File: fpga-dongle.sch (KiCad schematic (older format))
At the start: 118 parts, among them P1 CONN_01X02, P2 PGM, P3 right, P4 left, P5 CONN_01X40, P6 CONN_01X40, P7 DBG_SWD, P8 USB_PWR, Q1 BC857, SW1 T1107A(6x3,8x2,5MM)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

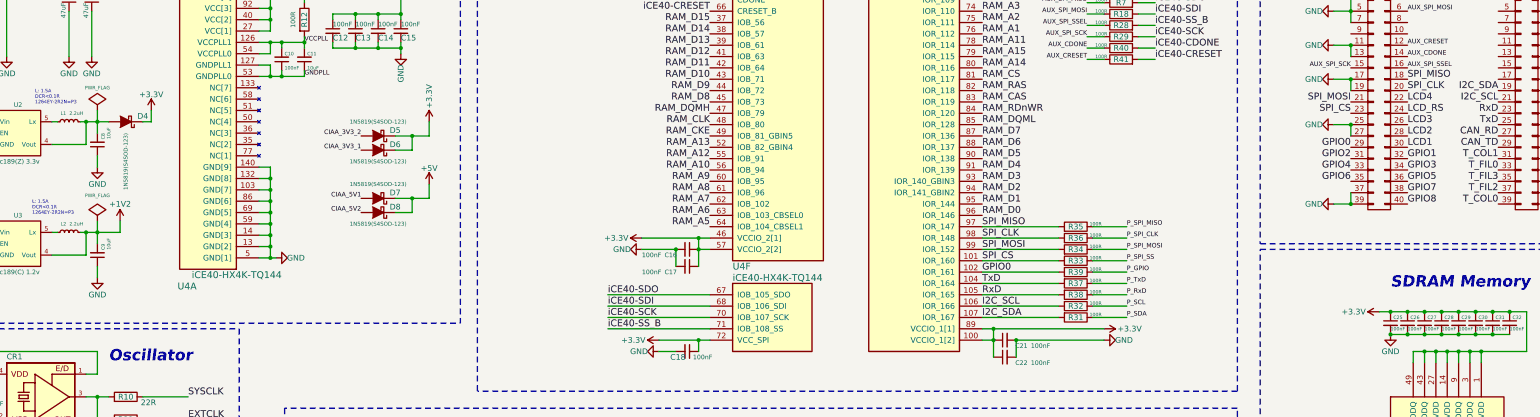
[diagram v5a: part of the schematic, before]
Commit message: Remove unnecesary components and clean power supply
Signed-off-by: Martin Ribelotta <martinribelotta@gmail.com>
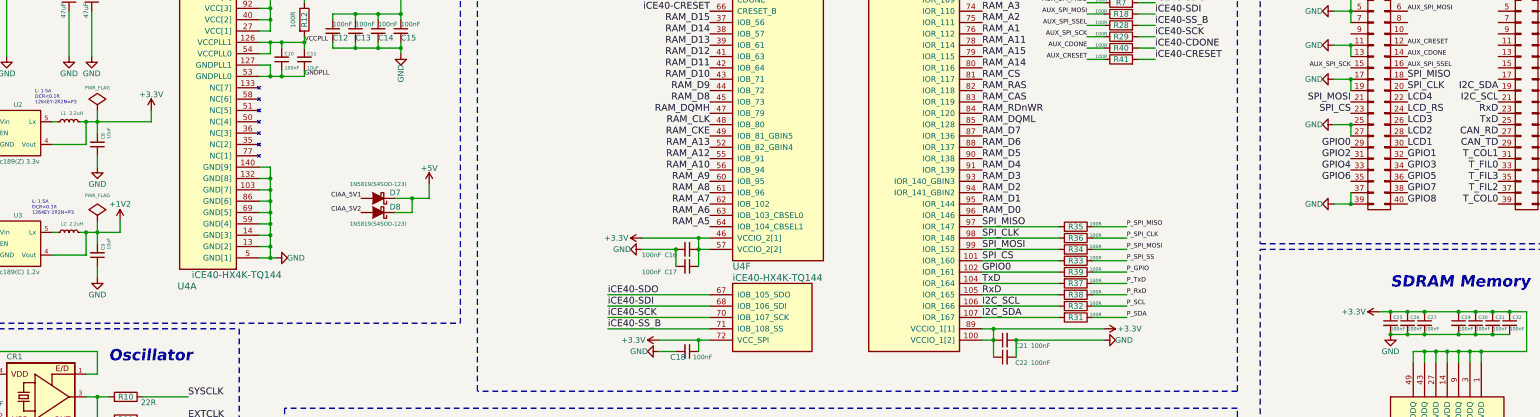
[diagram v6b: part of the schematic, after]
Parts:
- removed C28: 100nF, Capacitors_SMD:C_0805, symbol C_Small
- removed D4, D5, D6: 1N5819(S4SOD-123), Diodes_SMD:SOD-123, symbol D_Schottky
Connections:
- net +3V3: now also C8.2, L1.2, U2.4 (Vout)
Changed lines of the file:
@@
-$EndComp
-$Comp
-L C_Small C28
-U 1 1 57D74400
-P 14600 4375
-F 0 "C28" H 14625 4425 30  0000 L CNN
-F 1 "100nF" H 14600 4325 30  0000 L CNN
-F 2 "Capacitors_SMD:C_0805" H 14600 4375 50  0001 C CNN
-F 3 "" H 14600 4375 50  0000 C CNN
-	1    14600 4375
-	1    0    0    -1
 $EndComp
 $Comp
@@
 Connection ~ 14900 4275
 Connection ~ 14750 4275
-Connection ~ 14600 4275
 Connection ~ 14450 4275
 Connection ~ 14300 4275
@@
 Connection ~ 14550 7925
 Connection ~ 14450 7925
-Connection ~ 14600 4475
 Connection ~ 14750 4475
 Connection ~ 14900 4475
@@
 	2650 2800 2650 2600
 Wire Wire Line
-	2600 2600 2850 2600
+	2600 2600 3225 2600
 Connection ~ 2650 2600
 Wire Wire Line
@@
 Text Label 13800 1425 2    40   ~ 0
 CIAA_3V3_2
-Text Label 5075 2725 2    40   ~ 0
-CIAA_3V3_2
-Text Label 5075 2850 2    40   ~ 0
-CIAA_3V3_1
-$Comp
-L D_Schottky D4
-U 1 1 57F214FE
-P 3000 2600
-F 0 "D4" H 2850 2550 50  0000 C CNN
-F 1 "1N5819(S4SOD-123)" V 3000 2950 35  0000 C CNN
-F 2 "Diodes_SMD:SOD-123" H 3000 2600 60  0001 C CNN
-F 3 "" H 3000 2600 60  0000 C CNN
-	1    3000 2600
-	-1   0    0    1
-$EndComp
-Wire Wire Line
-	3225 2500 3225 2600
-Wire Wire Line
-	3225 2600 3150 2600
-$Comp
-L D_Schottky D5
-U 1 1 57F2204B
-P 5225 2725
-F 0 "D5" H 5075 2675 50  0000 C CNN
-F 1 "1N5819(S4SOD-123)" H 5225 2600 35  0000 C CNN
-F 2 "Diodes_SMD:SOD-123" H 5225 2725 60  0001 C CNN
-F 3 "" H 5225 2725 60  0000 C CNN
-	1    5225 2725
-	-1   0    0    1
-$EndComp
-$Comp
-L D_Schottky D6
-U 1 1 57F227C6
-P 5225 2850
-F 0 "D6" H 5075 2800 50  0000 C CNN
-F 1 "1N5819(S4SOD-123)" H 5225 2950 35  0000 C CNN
-F 2 "Diodes_SMD:SOD-123" H 5225 2850 60  0001 C CNN
-F 3 "" H 5225 2850 60  0000 C CNN
-	1    5225 2850
-	-1   0    0    1
-$EndComp
-Wire Wire Line
-	5375 2725 5675 2725
-Wire Wire Line
-	5525 2725 5525 2850
-Wire Wire Line
-	5525 2850 5375 2850
-Wire Wire Line
-	5675 2725 5675 2600
-Connection ~ 5525 2725
+Wire Wire Line
+	3225 2600 3225 2500
 $Comp
 L +3.3V #PWR092
-U 1 1 57F232E2
-P 5675 2600
-F 0 "#PWR092" H 5675 2450 50  0001 C CNN
-F 1 "+3.3V" V 5675 2825 50  0000 C CNN
-F 2 "" H 5675 2600 60  0000 C CNN
-F 3 "" H 5675 2600 60  0000 C CNN
-	1    5675 2600
-	-1   0    0    -1
-$EndComp
-$Comp
-L +3.3V #PWR093
 U 1 1 57F24EE1
 P 1450 3475
-F 0 "#PWR093" H 1450 3325 50  0001 C CNN
+F 0 "#PWR092" H 1450 3325 50  0001 C CNN
 F 1 "+3.3V" H 1450 3615 50  0000 C CNN
 F 2 "" H 1450 3475 60  0000 C CNN
@@
 CIAA_5V2
 $Comp
-L +5V #PWR094
+L +5V #PWR093
 U 1 1 57F2DD2B
 P 5675 3150
-F 0 "#PWR094" H 5675 3000 50  0001 C CNN
+F 0 "#PWR093" H 5675 3000 50  0001 C CNN
 F 1 "+5V" H 5675 3290 50  0000 C CNN
 F 2 "" H 5675 3150 60  0000 C CNN
@@
 	3200 1050 3200 1125
 $Comp
-L +5V #PWR095
+L +5V #PWR094
 U 1 1 57F32DD8
 P 12425 12625
-F 0 "#PWR095" H 12425 12475 50  0001 C CNN
+F 0 "#PWR094" H 12425 12475 50  0001 C CNN
 F 1 "+5V" H 12425 12765 50  0000 C CNN
 F 2 "" H 12425 12625 60  0000 C CNN
@@
 	12425 12625 12425 12700
 $Comp
-L +5V #PWR096
+L +5V #PWR095
 U 1 1 57F340DA
 P 1125 2100
-F 0 "#PWR096" H 1125 1950 50  0001 C CNN
+F 0 "#PWR095" H 1125 1950 50  0001 C CNN
 F 1 "+5V" H 1125 2240 50  0000 C CNN
 F 2 "" H 1125 2100 60  0000 C CNN
